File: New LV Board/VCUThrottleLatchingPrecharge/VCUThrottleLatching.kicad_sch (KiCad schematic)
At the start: 30 parts, among them J1 B12B-PH-K-S:JST_B12B-PH-K-S, Q1 SS8550, U1 IRLML2060TRPBF, U2 IRLML2060TRPBF, U3 IRLML2060TRPBF, U5 IRLML2060TRPBF, U6 IRLML2060TRPBF, U8 PMV160UP, U9 NE555D

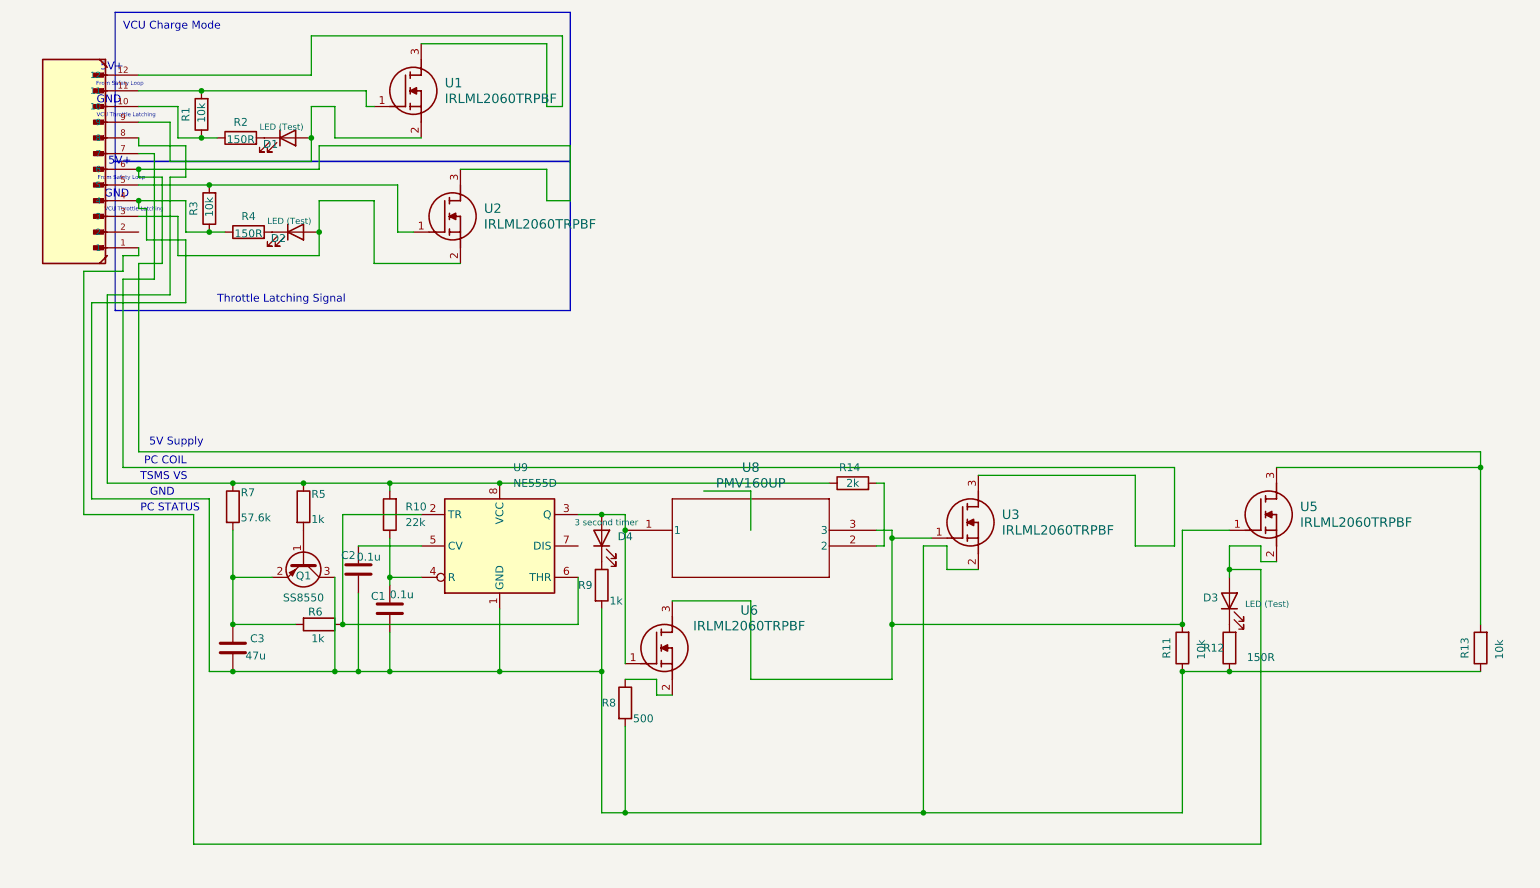
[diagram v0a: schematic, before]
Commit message: Precharge module added along with file name change
Precharge module added along with file name change
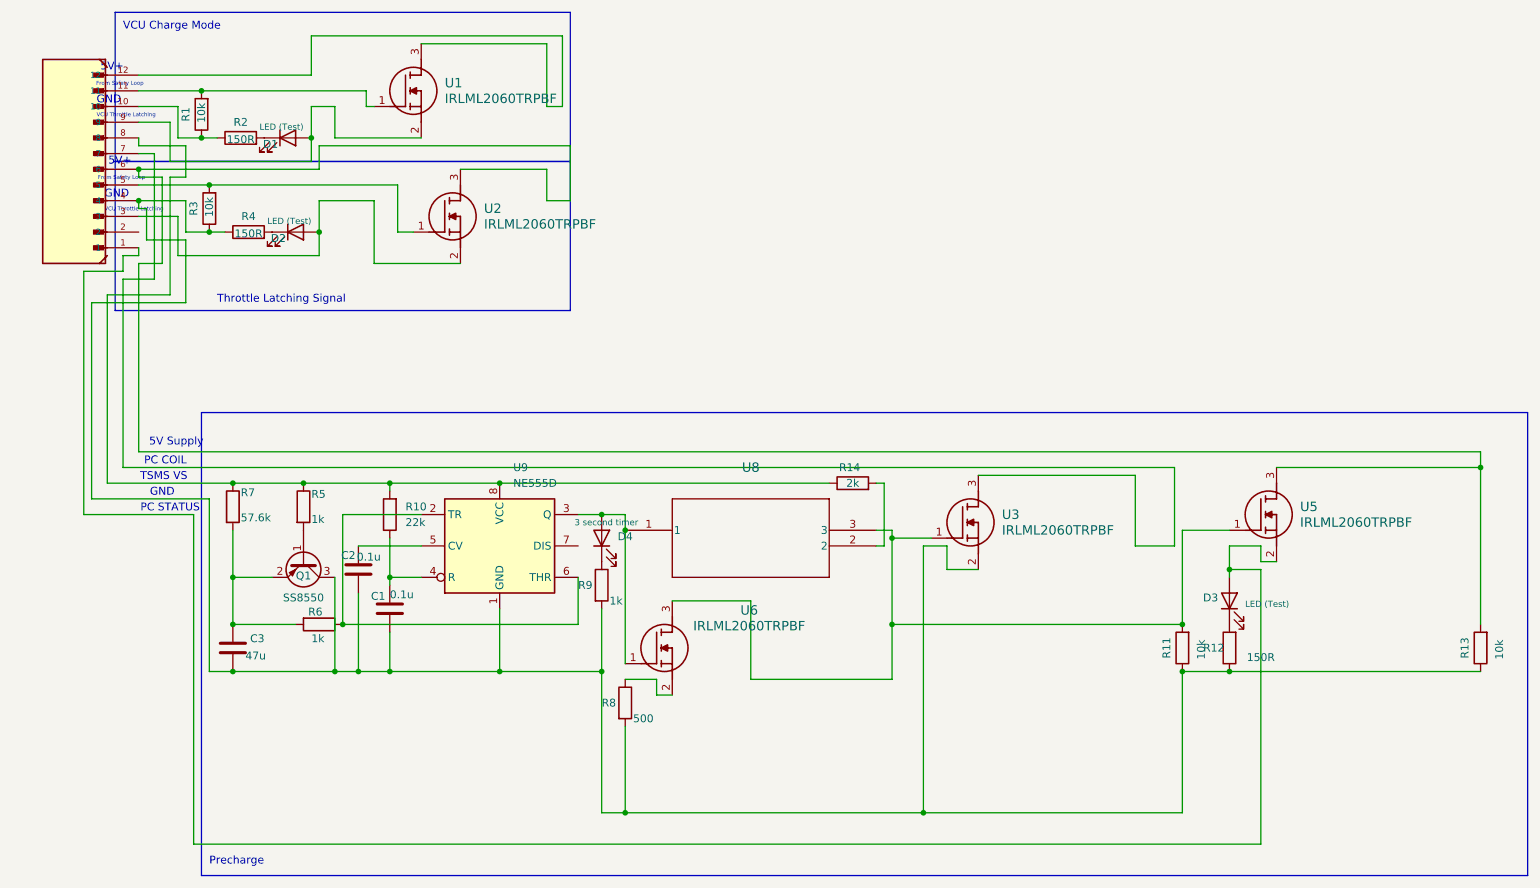
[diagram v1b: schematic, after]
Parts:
- C1: footprint Capacitor_SMD:C_0201_0603Metric -> Capacitor_SMD:C_1206_3216Metric_Pad1.33x1.80mm_HandSolder
- C2, C3: footprint Capacitor_SMD:C_0201_0603Metric -> C_1206_3216Metric_Pad1.33x1.80mm_HandSolder
- U8: footprint Footprints:SOIC127P599X175-8N -> Footprints:SOT95P237X112-3N
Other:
- note added: "Precharge"
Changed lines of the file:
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@@
 	)
 	(rectangle
+		(start 55.88 90.17)
+		(end 270.51 165.1)
+		(stroke
+			(width 0)
+			(type default)
+		)
+		(fill
+			(type none)
+		)
+	)
+	(rectangle
 		(start 41.91 49.53)
 		(end 115.57 73.66)
@@
 		)
 	)
+	(text "Precharge \n\n"
+		(exclude_from_sim no)
+		(at 57.15 165.608 0)
+		(effects
+			(font
+				(face "KiCad Font")
+				(size 1.27 1.27)
+			)
+			(justify left bottom)
+		)
+	)
 	(text "From Safety Loop\n"
 		(exclude_from_sim no)
@@
 	(wire
 		(pts
-			(xy 144.78 102.87) (xy 144.78 109.22)
-		)
-		(stroke
-			(width 0)
-			(type default)
-		)
-	)
-	(wire
-		(pts
 			(xy 124.46 133.35) (xy 129.54 133.35)
 		)
@@
 	(wire
 		(pts
-			(xy 137.16 102.87) (xy 144.78 102.87)
-		)
-		(stroke
-			(width 0)
-			(type default)
-		)
-	)
-	(wire
-		(pts
 			(xy 40.64 101.6) (xy 60.96 101.6)
 		)
@@
 			)
 		)
-		(property "Footprint" "Capacitor_SMD:C_0201_0603Metric"
+		(property "Footprint" "Capacitor_SMD:C_1206_3216Metric_Pad1.33x1.80mm_HandSolder"
 			(at 87.3252 125.73 0)
 			(effects
@@
 			)
 		)
-		(property "Footprint" "Capacitor_SMD:C_0201_0603Metric"
+		(property "Footprint" "C_1206_3216Metric_Pad1.33x1.80mm_HandSolder"
 			(at 82.2452 119.38 0)
 			(effects
@@
 					(size 1.524 1.524)
 				)
+				(hide yes)
 			)
 		)
-		(property "Footprint" "Footprints:SOIC127P599X175-8N"
+		(property "Footprint" "Footprints:SOT95P237X112-3N"
 			(at 124.46 109.22 0)
 			(effects
@@
 			)
 		)
-		(property "Footprint" "Capacitor_SMD:C_0201_0603Metric"
+		(property "Footprint" "C_1206_3216Metric_Pad1.33x1.80mm_HandSolder"
 			(at 61.9252 132.08 0)
 			(effects

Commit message: got carried away and made a new VCU throttle latching
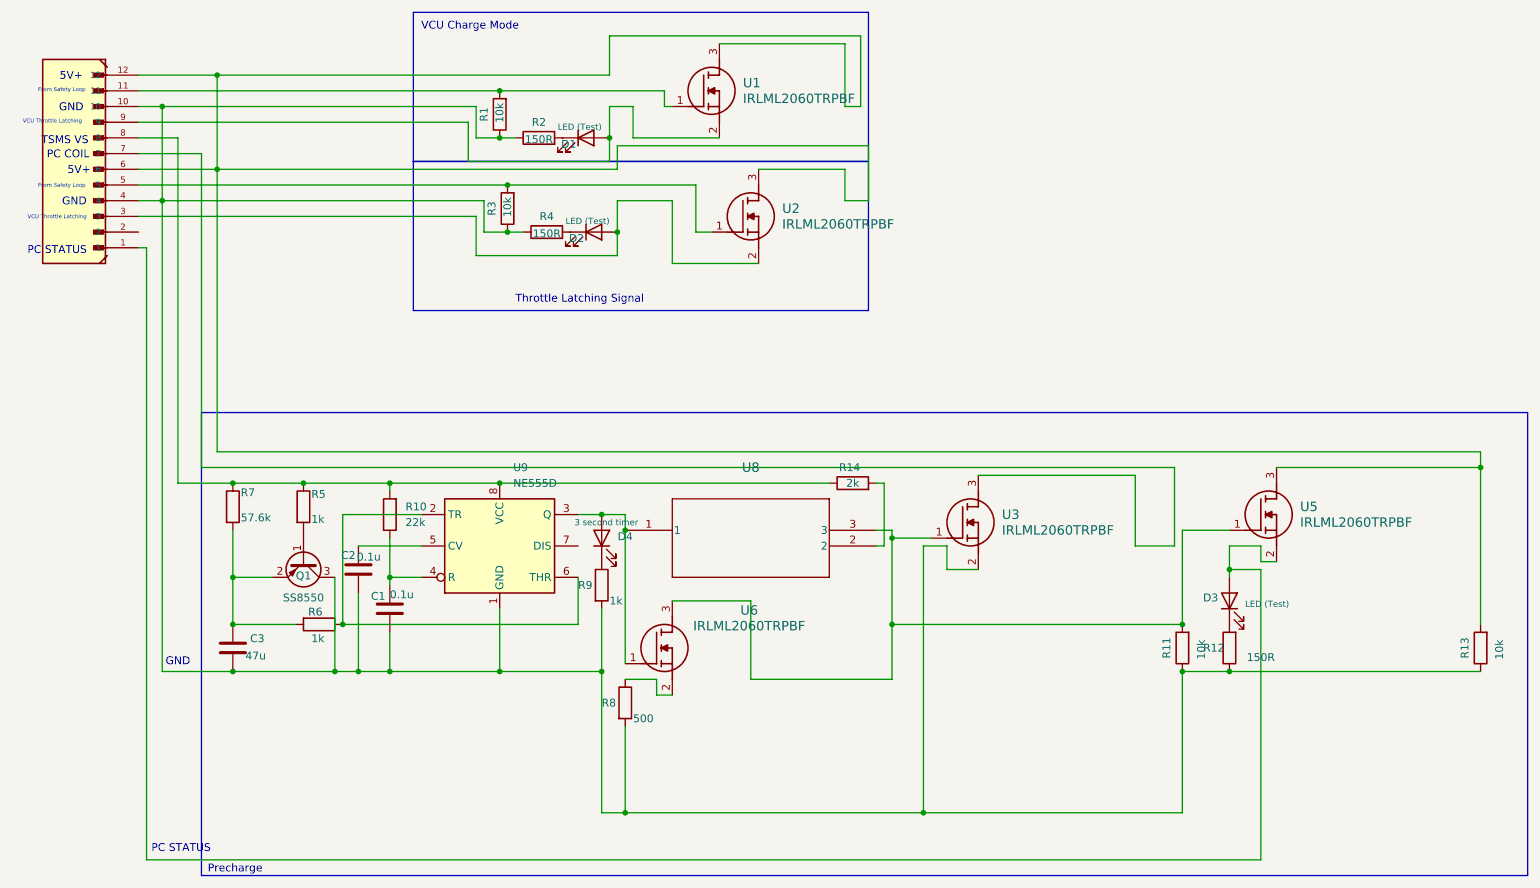
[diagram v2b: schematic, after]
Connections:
- net at C1.2, C2.2, C3.2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: now also J1.10, R1.1, R2.1
- net at J1.12, U1.3 (D): now also J1.6, R13.2, U2.3 (D), U5.3 (D)
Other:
- note removed: "5V Supply"
- moved on the sheet: D1, D2, R1, R2, R3, R4, U1, U2

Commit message: VCU Throttle Latching
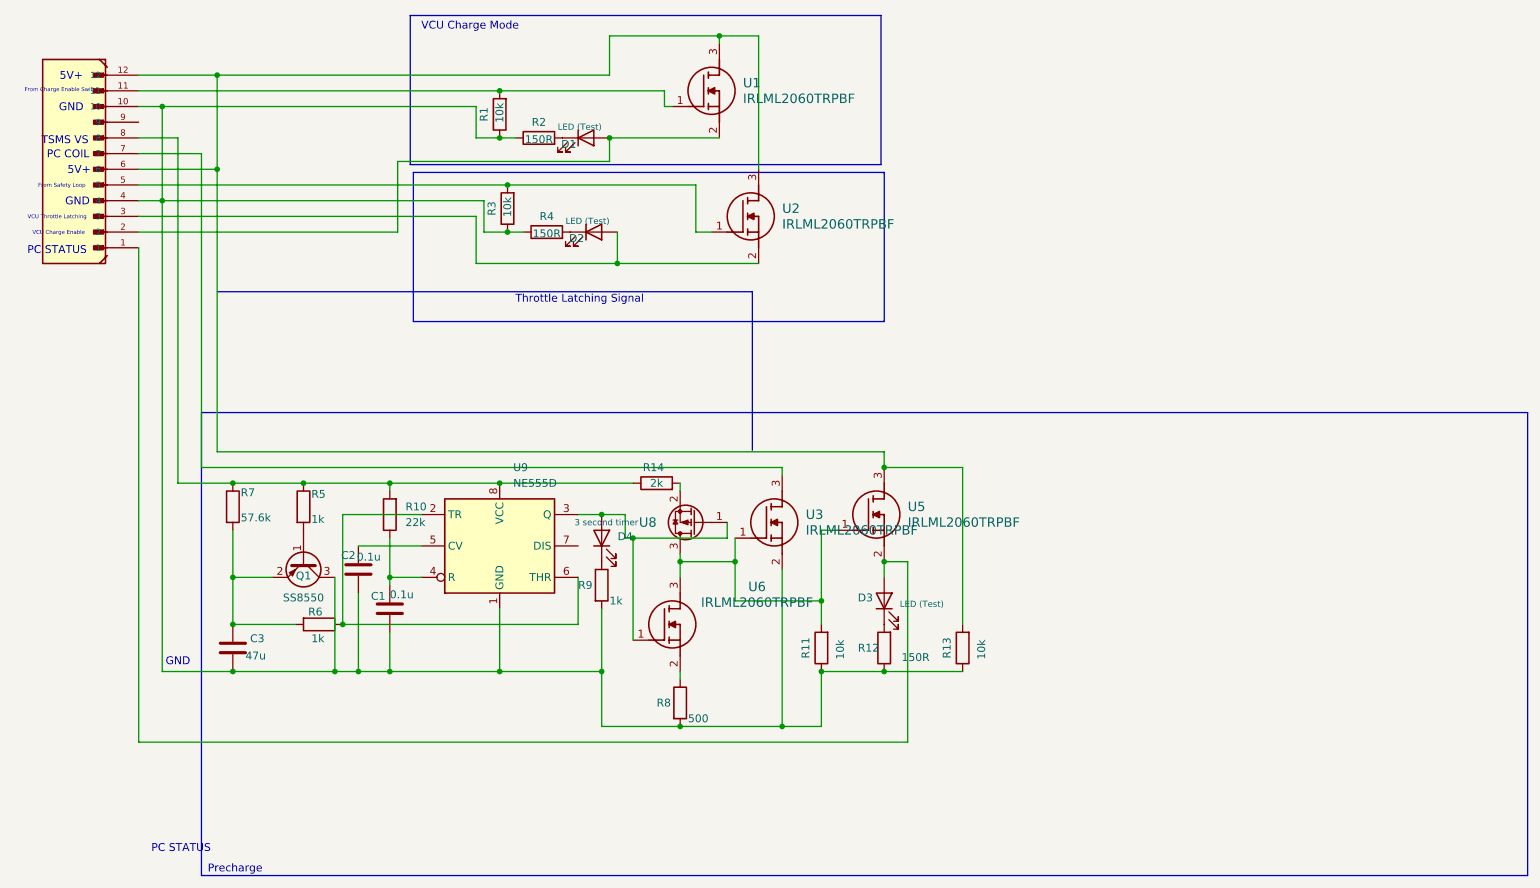
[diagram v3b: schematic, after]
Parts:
- U1, U2, U3, U5, U6: footprint SOT95P237X112-3N -> Package_TO_SOT_SMD:SOT-23-3
- U8: footprint Footprints:SOT95P237X112-3N -> Package_TO_SOT_SMD:SOT-23-3; symbol 2025-09-16_20-26-56:PMV160UP -> Transistor_FET:Q_PMOS_GSD
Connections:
- net at D1.2 (A), U1.2 (S): now also J1.2; no longer J1.9
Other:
- note added: "From Charge Enable Switch"
- note added: "VCU Charge Enable"
- moved on the sheet: D3, R11, R12, R13, R14, R8, U3, U5, U6
